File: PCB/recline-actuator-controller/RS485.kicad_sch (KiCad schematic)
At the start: 16 parts, among them J3 RJHSE-5381, U3 MAX3535ECWI+T

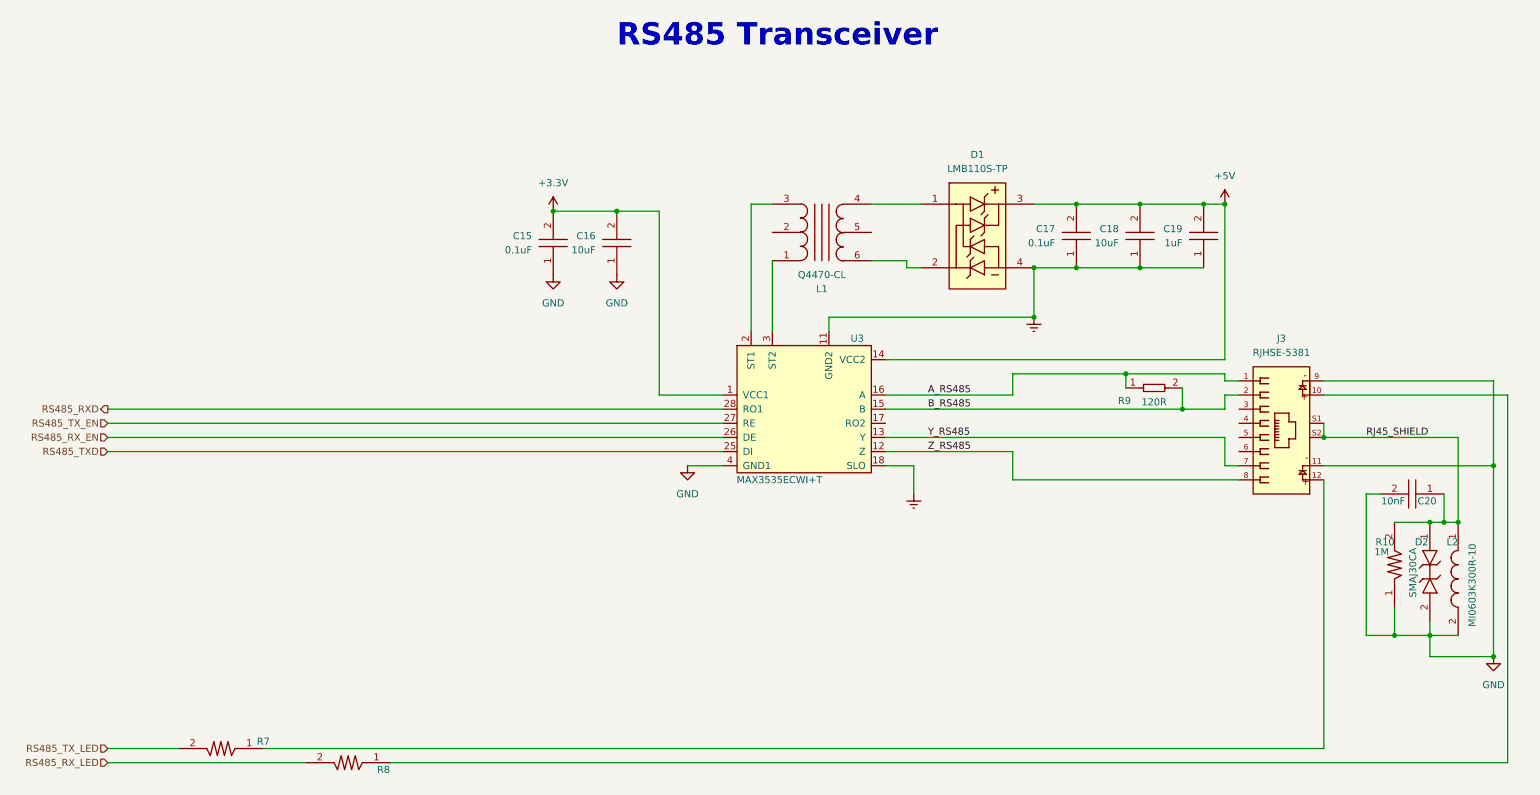
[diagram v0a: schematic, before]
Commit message: RS485
RS485 schematic corrected, 5V regulator removed.
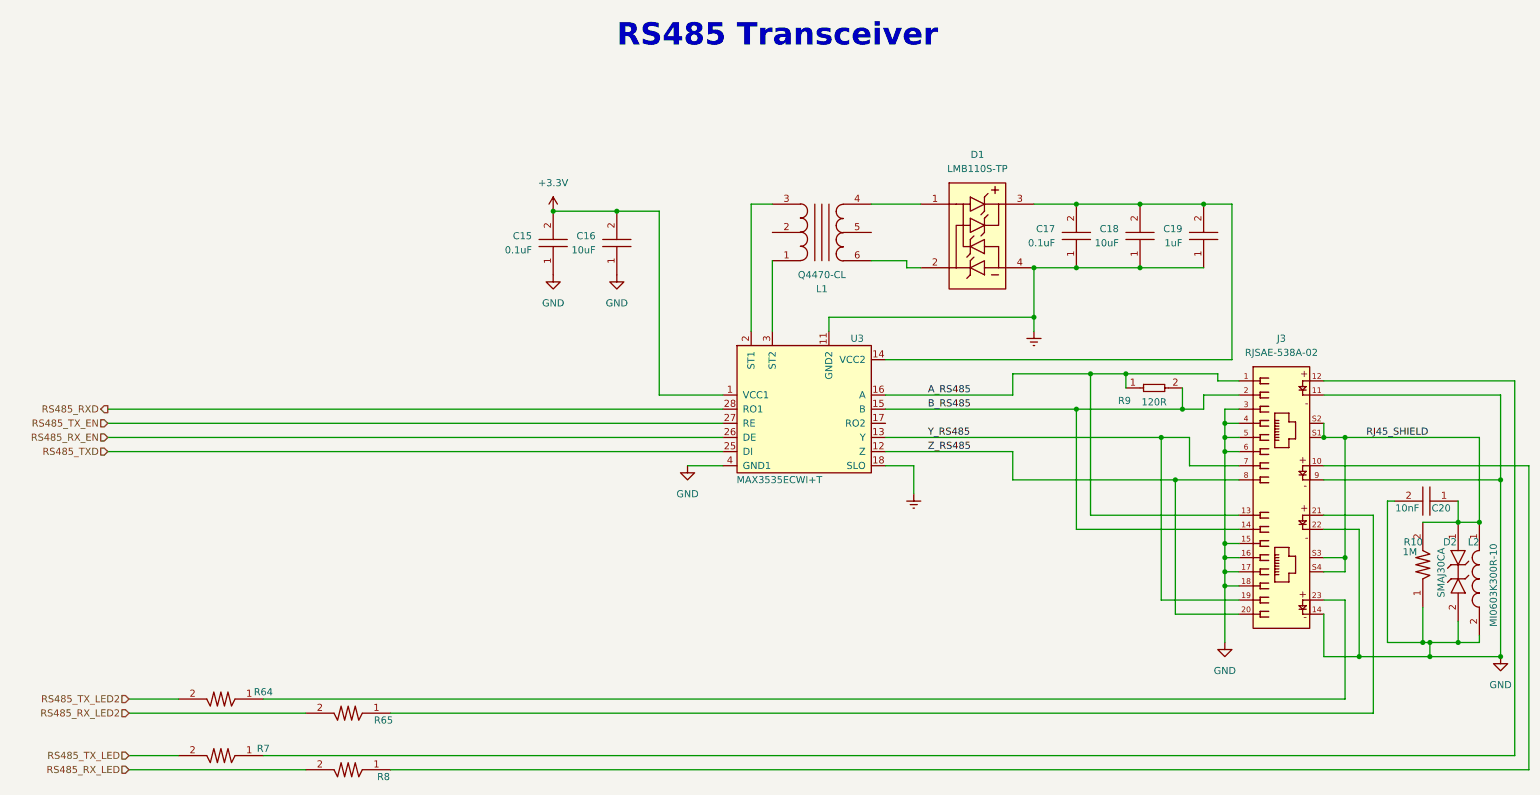
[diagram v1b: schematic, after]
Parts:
- removed J3: RJHSE-5381, AVR-KiCAD-Lib-Connectors:AMPHENOL_RJHSE-5381, symbol AVR-KiCAD-Lib-Connectors:RJHSE-5381
- added J3: RJSAE-538A-02, AVR-KiCAD-Lib-Connectors:AMPHENOL_RJSAE538A02, symbol AVR-KiCAD-Lib-Connectors:RJSAE-538A-02
- added R64, R65: RC0603FR-07470RL, AVR-KiCAD-Lib-Resistors:R0603, symbol AVR-KiCAD-Lib-Resistors:RC0603FR-07470RL
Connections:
- net A_RS485: now also J3.1, J3.13
- net B_RS485: now also J3.14, J3.2
- net GND: now also J3.11, J3.14, J3.15, J3.16, J3.17, J3.18, J3.22, J3.3, J3.4, J3.5, J3.6, J3.9
- net RJ45_SHIELD: now also J3.S1, J3.S2, J3.S3, J3.S4
- net Y_RS485: now also J3.19, J3.7
- net Z_RS485: now also J3.20, J3.8
- net at R8.1: now also J3.10
- net at R7.1: now also J3.12
- net +5V: no longer names the net of C17.2, C18.2, C19.2, D1.3, U3.14 (VCC2)
- new net: J3.21, R65.1
- new net: J3.23, R64.1
- new net RS485_RX_LED2: R65.2
- new net RS485_TX_LED2: R64.2
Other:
- moved on the sheet: C20, D2, L2, R10, R7, R8

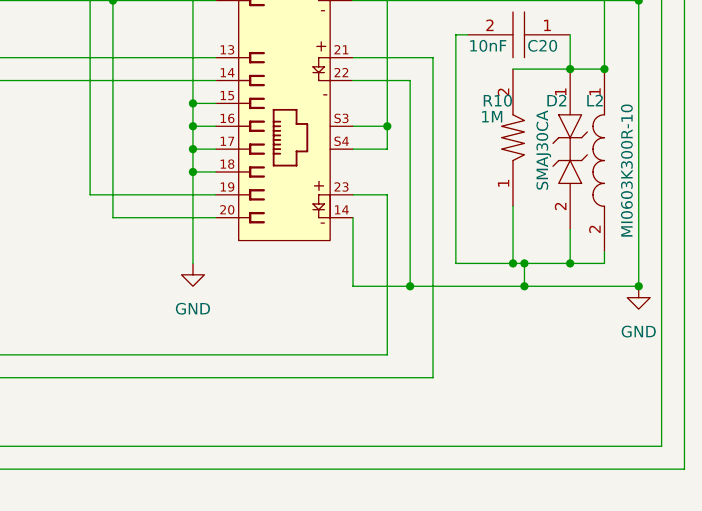
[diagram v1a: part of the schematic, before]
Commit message: RS485
RS485 circuit fixed and PCB topology updated.
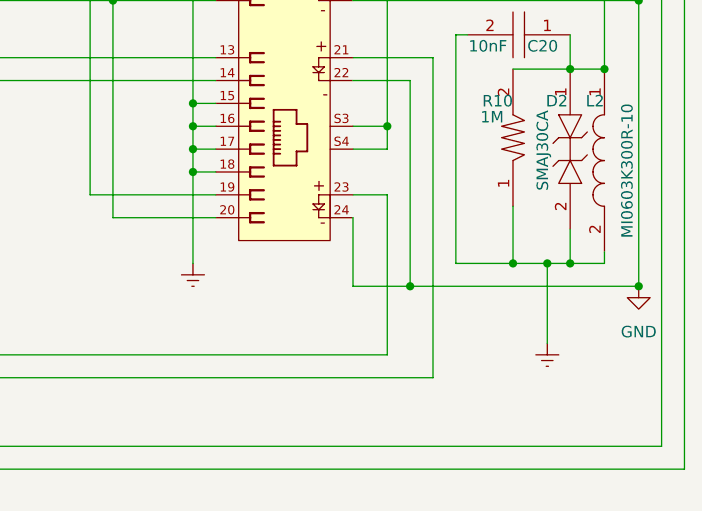
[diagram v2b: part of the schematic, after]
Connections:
- net Earth: now also C20.2, D2.2, J3.15, J3.16, J3.17, J3.18, J3.3, J3.4, J3.5, J3.6, L2.2, R10.1
- net GND: now also J3.24; no longer C20.2, D2.2, J3.14, J3.15, J3.16, J3.17, J3.18, J3.3, J3.4, J3.5, J3.6, L2.2, R10.1
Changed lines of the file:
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@@
 	)
 	(junction
-		(at 264.16 134.62)
-		(diameter 0)
-		(color 0 0 0 0)
-	)
-	(junction
 		(at 203.2 83.82)
 		(diameter 0)
@@
 	)
 	(junction
-		(at 264.16 132.08)
-		(diameter 0)
-		(color 0 0 0 0)
-	)
-	(junction
 		(at 193.04 73.66)
 		(diameter 0)
@@
 	)
 	(junction
+		(at 266.7 132.08)
+		(diameter 0)
+		(color 0 0 0 0)
+	)
+	(junction
 		(at 227.33 116.84)
 		(diameter 0)
@@
 	(wire
 		(pts
-			(xy 264.16 132.08) (xy 264.16 134.62)
-		)
-		(stroke
-			(width 0)
-			(type default)
-		)
-	)
-	(wire
-		(pts
 			(xy 248.92 95.25) (xy 245.11 95.25)
 		)
@@
 	(wire
 		(pts
-			(xy 264.16 132.08) (xy 262.89 132.08)
+			(xy 262.89 132.08) (xy 266.7 132.08)
 		)
 		(stroke
@@
 	(wire
 		(pts
-			(xy 251.46 134.62) (xy 264.16 134.62)
+			(xy 251.46 134.62) (xy 276.86 134.62)
 		)
 		(stroke
@@
 	(wire
 		(pts
-			(xy 193.04 64.77) (xy 200.66 64.77)
+			(xy 266.7 132.08) (xy 266.7 140.97)
 		)
 		(stroke
@@
 	(wire
 		(pts
-			(xy 245.11 119.38) (xy 248.92 119.38)
+			(xy 193.04 64.77) (xy 200.66 64.77)
 		)
 		(stroke
@@
 	(wire
 		(pts
-			(xy 281.94 100.33) (xy 281.94 154.94)
+			(xy 245.11 119.38) (xy 248.92 119.38)
 		)
 		(stroke
@@
 	(wire
 		(pts
-			(xy 264.16 132.08) (xy 269.24 132.08)
+			(xy 281.94 100.33) (xy 281.94 154.94)
 		)
 		(stroke
@@
 	(wire
 		(pts
+			(xy 266.7 132.08) (xy 269.24 132.08)
+		)
+		(stroke
+			(width 0)
+			(type default)
+		)
+	)
+	(wire
+		(pts
 			(xy 30.48 144.78) (xy 62.23 144.78)
 		)
@@
 	(wire
 		(pts
-			(xy 264.16 134.62) (xy 276.86 134.62)
-		)
-		(stroke
-			(width 0)
-			(type default)
-		)
-	)
-	(wire
-		(pts
 			(xy 229.87 127) (xy 218.44 127)
 		)
@@
 	)
 	(symbol
-		(lib_id "power:GND")
-		(at 227.33 132.08 0)
-		(unit 1)
-		(exclude_from_sim no)
-		(in_bom yes)
-		(on_board yes)
-		(dnp no)
-		(fields_autoplaced yes)
-		(property "Reference" "#PWR038"
-			(at 227.33 138.43 0)
-			(effects
-				(font
-					(size 1.27 1.27)
-				)
-				(hide yes)
-			)
-		)
-		(property "Value" "GND"
-			(at 227.33 137.16 0)
-			(effects
-				(font
-					(size 1.27 1.27)
-				)
-			)
-		)
-		(property "Footprint" ""
-			(at 227.33 132.08 0)
-			(effects
-				(font
-					(size 1.27 1.27)
-				)
-				(hide yes)
-			)
-		)
-		(property "Datasheet" ""
-			(at 227.33 132.08 0)
-			(effects
-				(font
-					(size 1.27 1.27)
-				)
-				(hide yes)
-			)
-		)
-		(property "Description" ""
-			(at 227.33 132.08 0)
-			(effects
-				(font
-					(size 1.27 1.27)
-				)
-				(hide yes)
-			)
-		)
-		(pin "1"
-		)
-		(instances
-			(project "recline-actuator-controller"
-				(path "/ebcf7e2b-8e27-4fda-b836-f1b7b461dd71/55f70b80-e6e7-47cf-83a5-15783fd4e573"
-					(reference "#PWR038")
-					(unit 1)
-				)
-			)
-		)
-	)
-	(symbol
 		(lib_id "AVR-KiCAD-Lib-Diodes:LMB110S-TP")
 		(at 177.8 67.31 0)
@@
 	)
 	(symbol
+		(lib_id "power:Earth")
+		(at 266.7 140.97 0)
+		(unit 1)
+		(exclude_from_sim no)
+		(in_bom yes)
+		(on_board yes)
+		(dnp no)
+		(fields_autoplaced yes)
+		(property "Reference" "#PWR031"
+			(at 266.7 147.32 0)
+			(effects
+				(font
+					(size 1.27 1.27)
+				)
+				(hide yes)
+			)
+		)
+		(property "Value" "Earth"
+			(at 266.7 144.78 0)
+			(effects
+				(font
+					(size 1.27 1.27)
+				)
+				(hide yes)
+			)
+		)
+		(property "Footprint" ""
+			(at 266.7 140.97 0)
+			(effects
+				(font
+					(size 1.27 1.27)
+				)
+				(hide yes)
+			)
+		)
+		(property "Datasheet" "~"
+			(at 266.7 140.97 0)
+			(effects
+				(font
+					(size 1.27 1.27)
+				)
+				(hide yes)
+			)
+		)
+		(property "Description" ""
+			(at 266.7 140.97 0)
+			(effects
+				(font
+					(size 1.27 1.27)
+				)
+				(hide yes)
+			)
+		)
+		(pin "1"
+		)
+		(instances
+			(project "recline-actuator-controller"
+				(path "/ebcf7e2b-8e27-4fda-b836-f1b7b461dd71/55f70b80-e6e7-47cf-83a5-15783fd4e573"
+					(reference "#PWR031")
+					(unit 1)
+				)
+			)
+		)
+	)
+	(symbol
 		(lib_id "AVR-KiCAD-Lib-Connectors:RJSAE-538A-02")
 		(at 232.41 82.55 0)
@@
 		(pin "4"
 		)
-		(pin "14"
+		(pin "24"
 		)
 		(pin "7"
@@
 					(unit 1)
 				)
+			)
+		)
+	)
+	(symbol
+		(lib_id "power:Earth")
+		(at 227.33 132.08 0)
+		(unit 1)
+		(exclude_from_sim no)
+		(in_bom yes)
+		(on_board yes)
+		(dnp no)
+		(fields_autoplaced yes)
+		(property "Reference" "#PWR025"
+			(at 227.33 138.43 0)
+			(effects
+				(font
+					(size 1.27 1.27)
+				)
+				(hide yes)
+			)
+		)
+		(property "Value" "Earth"
+			(at 227.33 135.89 0)
+			(effects
+				(font
+					(size 1.27 1.27)
+				)
+				(hide yes)
+			)
+		)
+		(property "Footprint" ""
+			(at 227.33 132.08 0)
+			(effects
+				(font
+					(size 1.27 1.27)
+				)
+				(hide yes)
+			)
+		)
+		(property "Datasheet" "~"
+			(at 227.33 132.08 0)
+			(effects
+				(font
+					(size 1.27 1.27)
+				)
+				(hide yes)
+			)
+		)
+		(property "Description" ""
+			(at 227.33 132.08 0)
+			(effects
+				(font
+					(size 1.27 1.27)
+				)
+				(hide yes)
+			)
+		)
+		(pin "1"
+		)
+		(instances
+			(project "recline-actuator-controller"
+				(path "/ebcf7e2b-8e27-4fda-b836-f1b7b461dd71/55f70b80-e6e7-47cf-83a5-15783fd4e573"
+					(reference "#PWR025")
+					(unit 1)
+				)
